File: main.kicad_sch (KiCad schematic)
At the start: 34 parts, among them J1 USB_C_Receptacle_USB2.0_14P, SW1 SW_PUSH, SW2 SW_PUSH, SW3 SW_PUSH, SW4 SW_PUSH, SW5 SW_PUSH, U1 NCP1117-3.3_SOT223, U2 RP2040, U3 W25Q128JVS, Y1 ABM8-272-T3

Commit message: :sparkles: (all) prepare fab
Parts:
- removed C10: 10u, Capacitor_SMD:C_0805_2012Metric, symbol Device:C
- removed C17: 33p, Capacitor_SMD:C_0402_1005Metric, symbol Device:C
- removed R6: 1k, Resistor_SMD:R_0402_1005Metric, symbol Device:R
- removed SW1, SW2: SW_PUSH, kamo3_footprint:SW_CherryMX_Hotswap_1.25u, symbol kbd:SW_PUSH
- removed SW4: SW_PUSH, kamo3_footprint:Tact_Switch_5.1_5.1mm_SMD, symbol kamo3_symbol:SW_Push_4pin
- added C4: 10u, Capacitor_SMD:C_0805_2012Metric, symbol Device:C
- added D1, D2, D3, D4, D5, D6, D7, D8, D9: D, kamo3_footprint:Diode_SOD123, symbol Device:D
- added R1: 10k, Resistor_SMD:R_0402_1005Metric, symbol Device:R
- added R4: 1k, Resistor_SMD:R_0402_1005Metric, symbol Device:R
- added SW1: SW_PUSH, kamo3_footprint:Tact_Switch_5.1_5.1mm_SMD, symbol kamo3_symbol:SW_Push_4pin
- added SW10, SW4, SW5, SW6, SW7, SW8, SW9: SW_PUSH, kamo3_footprint:SW_ChocV1_Hotswap_1.0u, symbol kbd:SW_PUSH
- added SW11: SW_PUSH, kamo3_footprint:SW_ChocV1_Hotswap_1.50u, symbol kbd:SW_PUSH
- added SW12: RotaryEncoder, Rotary_Encoder:RotaryEncoder_Alps_EC12E_Vertical_H20mm, symbol Device:RotaryEncoder
- C15: value 10u -> 30p; footprint Capacitor_SMD:C_0805_2012Metric -> Capacitor_SMD:C_0603_1608Metric; LCSC C15850 -> C1658
- C16: value 33p -> 30p; footprint Capacitor_SMD:C_0402_1005Metric -> Capacitor_SMD:C_0603_1608Metric; LCSC C1562 -> C1658
- R5: renamed from R3; footprint Resistor_SMD:R_0402_1005Metric -> Resistor_SMD:R_0603_1608Metric; LCSC C321419 -> C25190
- R6: renamed from R4; footprint Resistor_SMD:R_0402_1005Metric -> Resistor_SMD:R_0603_1608Metric; LCSC C321419 -> C25190
- R7: renamed from R5; LCSC C17168 -> (none)
- SW3: footprint kamo3_footprint:SW_CherryMX_Hotswap_1.00u -> kamo3_footprint:SW_ChocV1_Hotswap_1.0u
- renumbered C6 to C10, C7 to C11, C8 to C12, C9 to C13, C12 to C3, C11 to C5, C3 to C6, C13 to C7, C4 to C8, C5 to C9, R1 to R3, R7 to R8, SW5 to SW2
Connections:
- net +3V3: now also R1.1; no longer C15.1
- net GND: now also C15.1, C16.1, R2.1, R3.1, C4.2, SW1.1, SW1.2, SW12.C; no longer C15.2, C16.2, R2.2, R3.2, SW3.2
- net QSPI_SS: now also R4.1
- net VBUS: now also C4.1
- net XIN: now also C15.2; no longer C16.1
- net at R8.2, Y1.3: now also C16.2
- net at U2.4 (GPIO2): no longer SW3.1
- net at U2.26 (RUN): now also R1.2, SW1.3, SW1.4
- net enc_a: now reaches U2.11 (GPIO8)
- net enc_a: now also SW12.A
- net enc_b: now reaches U2.12 (GPIO9)
- net enc_b: now also SW12.B
- net row1: now reaches U2.29 (GPIO18)
- net row1: now also D2.1 (K), D4.1 (K), D6.1 (K), D8.1 (K), D9.1 (K)
- net row0: now reaches U2.30 (GPIO19)
- net row0: now also D1.1 (K), D3.1 (K), D5.1 (K), D7.1 (K)
- net col4: now reaches U2.37 (GPIO25)
- net col4: now also SW11.1
- net col3: now reaches U2.38 (GPIO26_ADC0)
- net col3: now also SW10.1, SW9.1
- net col2: now reaches U2.39 (GPIO27_ADC1)
- net col2: now also SW7.1, SW8.1
- net col1: now reaches U2.40 (GPIO28_ADC2)
- net col1: now also SW5.1, SW6.1
- net col0: now reaches U2.41 (GPIO29_ADC3)
- net col0: now also SW3.1, SW4.1
- net ~{USB_BOOT}: no longer names the net of SW2.3, SW2.4
- net ~{USB_BOOT}: now also R4.2
- new net: D3.2 (A), SW5.2
- new net: D5.2 (A), SW7.2
- new net: D2.2 (A), SW4.2
- new net: D7.2 (A), SW9.2
- new net: D6.2 (A), SW8.2
- new net: J1.B5 (CC2), R2.2
- new net: D8.2 (A), SW10.2
- new net: J1.A5 (CC1), R3.2
- new net: D1.2 (A), SW3.2
- new net: D4.2 (A), SW6.2
- new net: D9.2 (A), SW11.2
- no-connect marks 29 -> 23
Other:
- note added: "Make sure C3 is close to pin 45 of RP2040"
- note added: "Make sure C7 is close to pin 44 of RP2040"
- note added: "Make sure R5 and R6 are close to RP2040"
- note added: "RP2040"
- note removed: "Make sure C10 is close to pin 44 of RP2040"
- note removed: "Make sure C8 is close to pin 45 of RP2040"
- note removed: "Make sure R3 and R4 are close to RP2040"
- moved on the sheet: C1, C10, C11, C12, C13, C2, C3, C5, C6, C7, C8, C9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

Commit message: :bug: (chore)
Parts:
- SW1: value SW_PUSH -> RESET
- SW2: value SW_PUSH -> BOOT
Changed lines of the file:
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@@
 			)
 		)
-		(property "Value" "SW_PUSH"
+		(property "Value" "BOOT"
 			(at 142.24 59.6899 90)
 			(effects
@@
 			)
 		)
-		(property "Value" "SW_PUSH"
+		(property "Value" "RESET"
 			(at 52.07 209.5499 90)
 			(effects

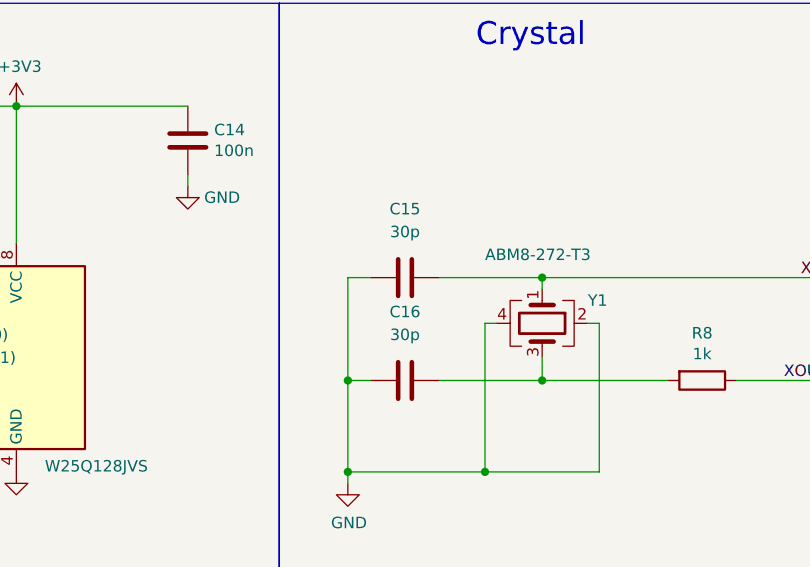
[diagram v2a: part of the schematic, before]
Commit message: :bug: (fix capacitor)
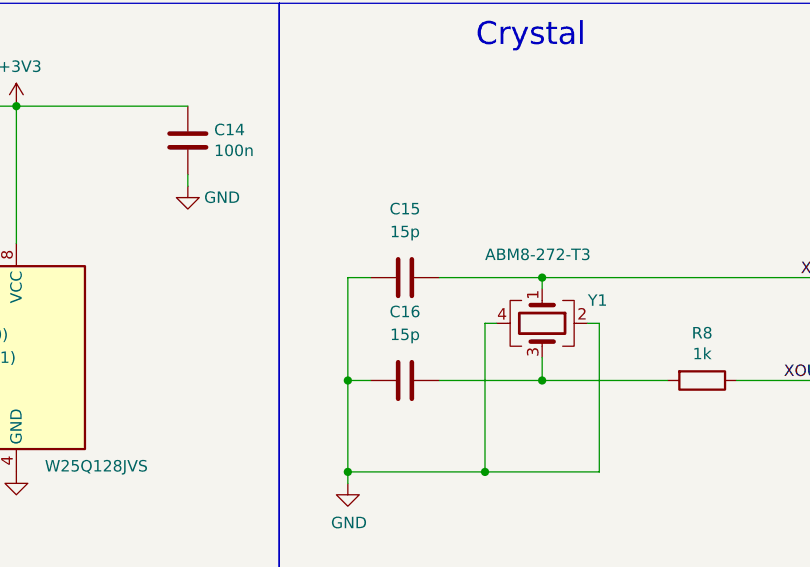
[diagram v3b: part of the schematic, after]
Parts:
- C15, C16: value 30p -> 15p; LCSC C1658 -> C1644
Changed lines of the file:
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@@
 			)
 		)
-		(property "Value" "30p"
+		(property "Value" "15p"
 			(at 226.06 39.37 90)
 			(effects
@@
 			)
 		)
-		(property "LCSC" "C1658"
+		(property "LCSC" "C1644"
 			(at 226.06 44.45 0)
 			(effects
@@
 			)
 		)
-		(property "Value" "30p"
+		(property "Value" "15p"
 			(at 226.06 50.8 90)
 			(effects
@@
 			)
 		)
-		(property "LCSC" "C1658"
+		(property "LCSC" "C1644"
 			(at 226.06 55.88 0)
 			(effects
